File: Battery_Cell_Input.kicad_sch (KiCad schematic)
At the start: 27 parts, among them J1101 Battery_1, J1102 Conn_01x02, Q1101 NMOS, Q1102 NMOS, U1101 BQ76920PW

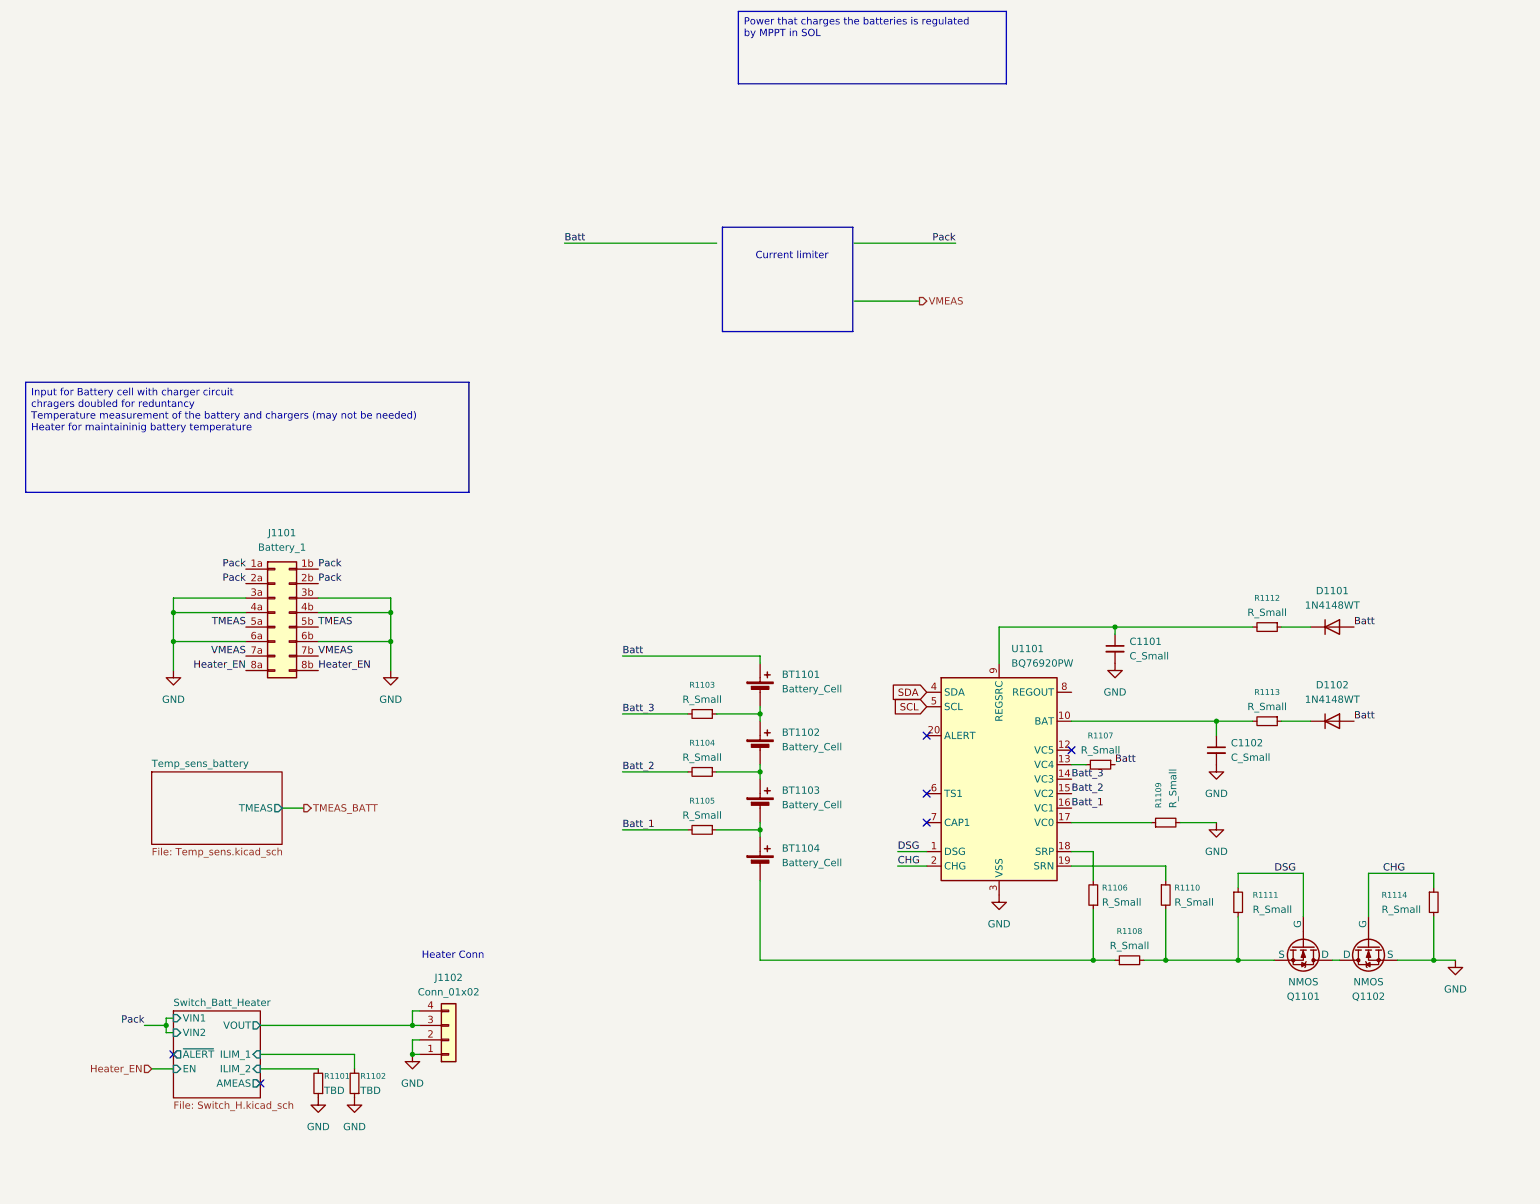
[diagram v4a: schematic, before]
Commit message: updated battery pack module; updated solar inputs module
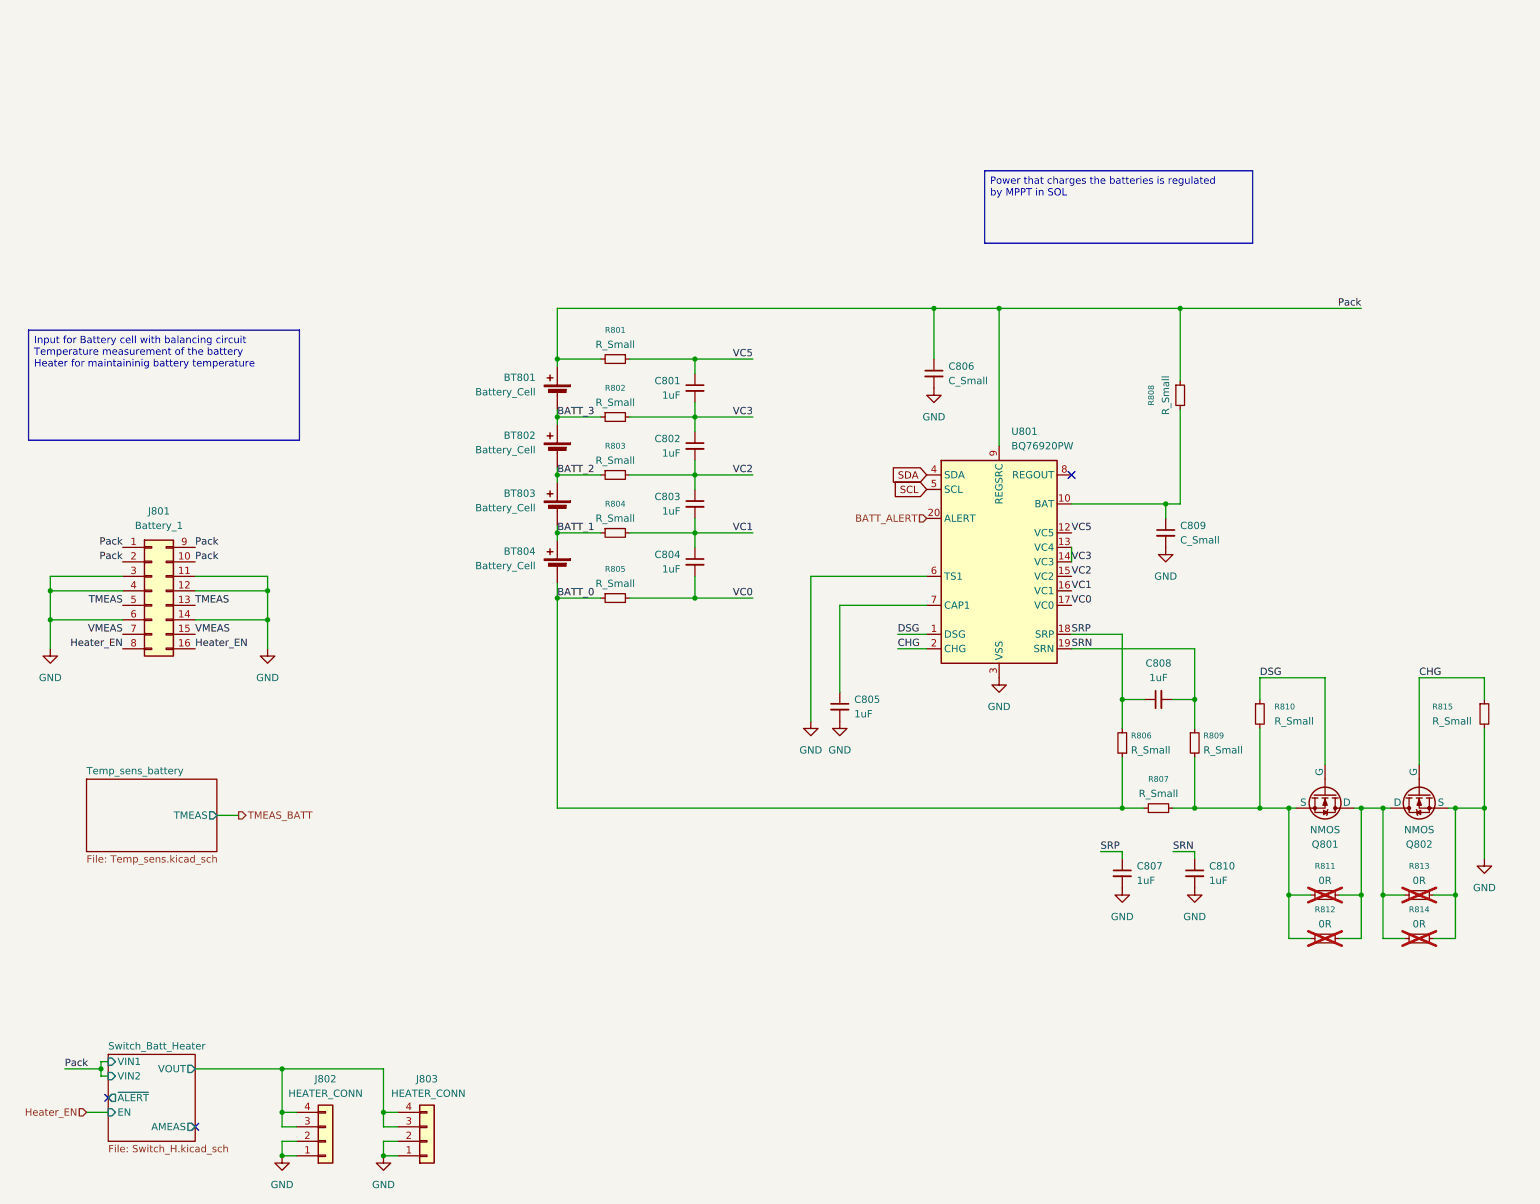
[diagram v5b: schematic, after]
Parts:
- removed D1101, D1102: 1N4148WT, Diode_SMD:D_SOD-523, symbol Diode:1N4148WT
- removed R1101, R1102: TBD, Resistor_SMD:R_0603_1608Metric_Pad0.98x0.95mm_HandSolder, symbol Device:R_Small
- removed R1109, R1112: R_Small, Resistor_SMD:R_0603_1608Metric_Pad0.98x0.95mm_HandSolder, symbol Device:R_Small
- added C801, C802, C803, C804, C805, C807, C808, C810: 1uF, Capacitor_SMD:C_0603_1608Metric_Pad1.08x0.95mm_HandSolder, symbol Device:C_Small
- added J803: HEATER_CONN, symbol Connector_Generic:Conn_01x04
- added R805: R_Small, Resistor_SMD:R_0603_1608Metric_Pad0.98x0.95mm_HandSolder, symbol Device:R_Small
- added R811, R812, R813, R814: 0R, Resistor_SMD:R_0603_1608Metric_Pad0.98x0.95mm_HandSolder, symbol Device:R_Small
- BT801: renamed from BT1101; footprint (none) -> Outlines:BHC186501P-li-ion
- BT802: renamed from BT1102; footprint (none) -> Outlines:BHC186501P-li-ion
- BT803: renamed from BT1103; footprint (none) -> Outlines:BHC186501P-li-ion
- BT804: renamed from BT1104; footprint (none) -> Outlines:BHC186501P-li-ion
- J801: renamed from J1101; symbol Connector_Generic:Conn_02x08_Row_Letter_Last -> Connector_Generic:Conn_02x08_Top_Bottom
- J802: renamed from J1102; value Conn_01x02 -> HEATER_CONN
- Q801: renamed from Q1101; footprint Package_TO_SOT_SMD:SOT-23-6 -> Outlines:NVTFS5116PLTWG
- Q802: renamed from Q1102; footprint Package_TO_SOT_SMD:SOT-23-6 -> Outlines:NVTFS5116PLTWG
- renumbered C1101 to C806, C1102 to C809, R1107 to R801, R1103 to R802, R1104 to R803, R1105 to R804, R1106 to R806, R1108 to R807, R1113 to R808, R1110 to R809, R1111 to R810, R1114 to R815, U1101 to U801
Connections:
- net Batt_3 is gone; now on net VC3: R802.2, U801.14 (VC3)
- net GND: now also J801.11 (Pin_11), J801.12 (Pin_12), J801.14 (Pin_14), J801.3 (Pin_3), J801.4 (Pin_4), J801.6 (Pin_6), U801.6 (TS1), C805.2, C807.2, C810.2, J803.1 (Pin_1), J803.2 (Pin_2), R813.2, R814.2; no longer J801.3a (Pin_3a), J801.3b (Pin_3b), J801.4a (Pin_4a), J801.4b (Pin_4b), J801.6a (Pin_6a), J801.6b (Pin_6b)
- net Heater_EN: now also J801.16 (Pin_16), J801.8 (Pin_8); no longer J801.8a (Pin_8a), J801.8b (Pin_8b)
- net Pack: now also BT801.1 (+), C806.1, J801.1 (Pin_1), J801.10 (Pin_10), J801.2 (Pin_2), J801.9 (Pin_9), R801.2, R808.1, U801.9 (REGSRC); no longer J801.1a (Pin_1a), J801.1b (Pin_1b), J801.2a (Pin_2a), J801.2b (Pin_2b)
- net Switch_Batt_Heater/VOUT: now also J803.3 (Pin_3), J803.4 (Pin_4)
- net TMEAS: now also J801.13 (Pin_13), J801.5 (Pin_5); no longer J801.5a (Pin_5a), J801.5b (Pin_5b)
- net VMEAS: now also J801.15 (Pin_15), J801.7 (Pin_7); no longer J801.7a (Pin_7a), J801.7b (Pin_7b)
- net at Q801.3 (S), R807.2, R809.2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: now also R811.1, R812.1
- net SRN: now reaches R809.1, U801.19 (SRN)
- net SRN: now also C808.2, C810.1
- net BATT_1: now reaches BT803.2 (-), BT804.1 (+), R804.1
- net at Q801.1 (D), Q802.1 (D): now also R811.2, R812.2, R813.1, R814.1
- net BATT_2: now reaches BT802.2 (-), BT803.1 (+), R803.1
- net BATT_0: now reaches BT804.2 (-), R806.1, R807.1
- net BATT_0: now also R805.1
- net BATT_3: now reaches BT801.2 (-), BT802.1 (+), R802.1
- net VC5: now reaches U801.12 (VC5)
- net VC5: now also R801.1, C801.1
- net VC3: now reaches U801.13 (VC4)
- net VC3: now also C801.2, C802.1; no longer R801.2
- net VC0: now reaches U801.17 (VC0)
- net VC0: now also C804.2, R805.2
- net SRP: now reaches R806.2, U801.18 (SRP)
- net SRP: now also C807.1, C808.1
- net BATT_ALERT: now reaches U801.20 (ALERT)
- net at U801.7 (CAP1): now also C805.1
- removed net Batt: BT801.1 (+), R801.1
- net Batt_1 renamed VC1
- net VC1: now also C803.2, C804.1
- net Batt_2 renamed VC2
- net VC2: now also C802.2, C803.1
- no-connect marks 6 -> 3
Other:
- sheet Switch_Batt_Heater ports: added none; removed ILIM_1, ILIM_2
- note removed: "Current limiter"
- note removed: "Heater Conn"
- moved on the sheet: BT801, BT802, BT803, BT804, C806, C809, J801, J802, Q801, Q802, R801, R802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

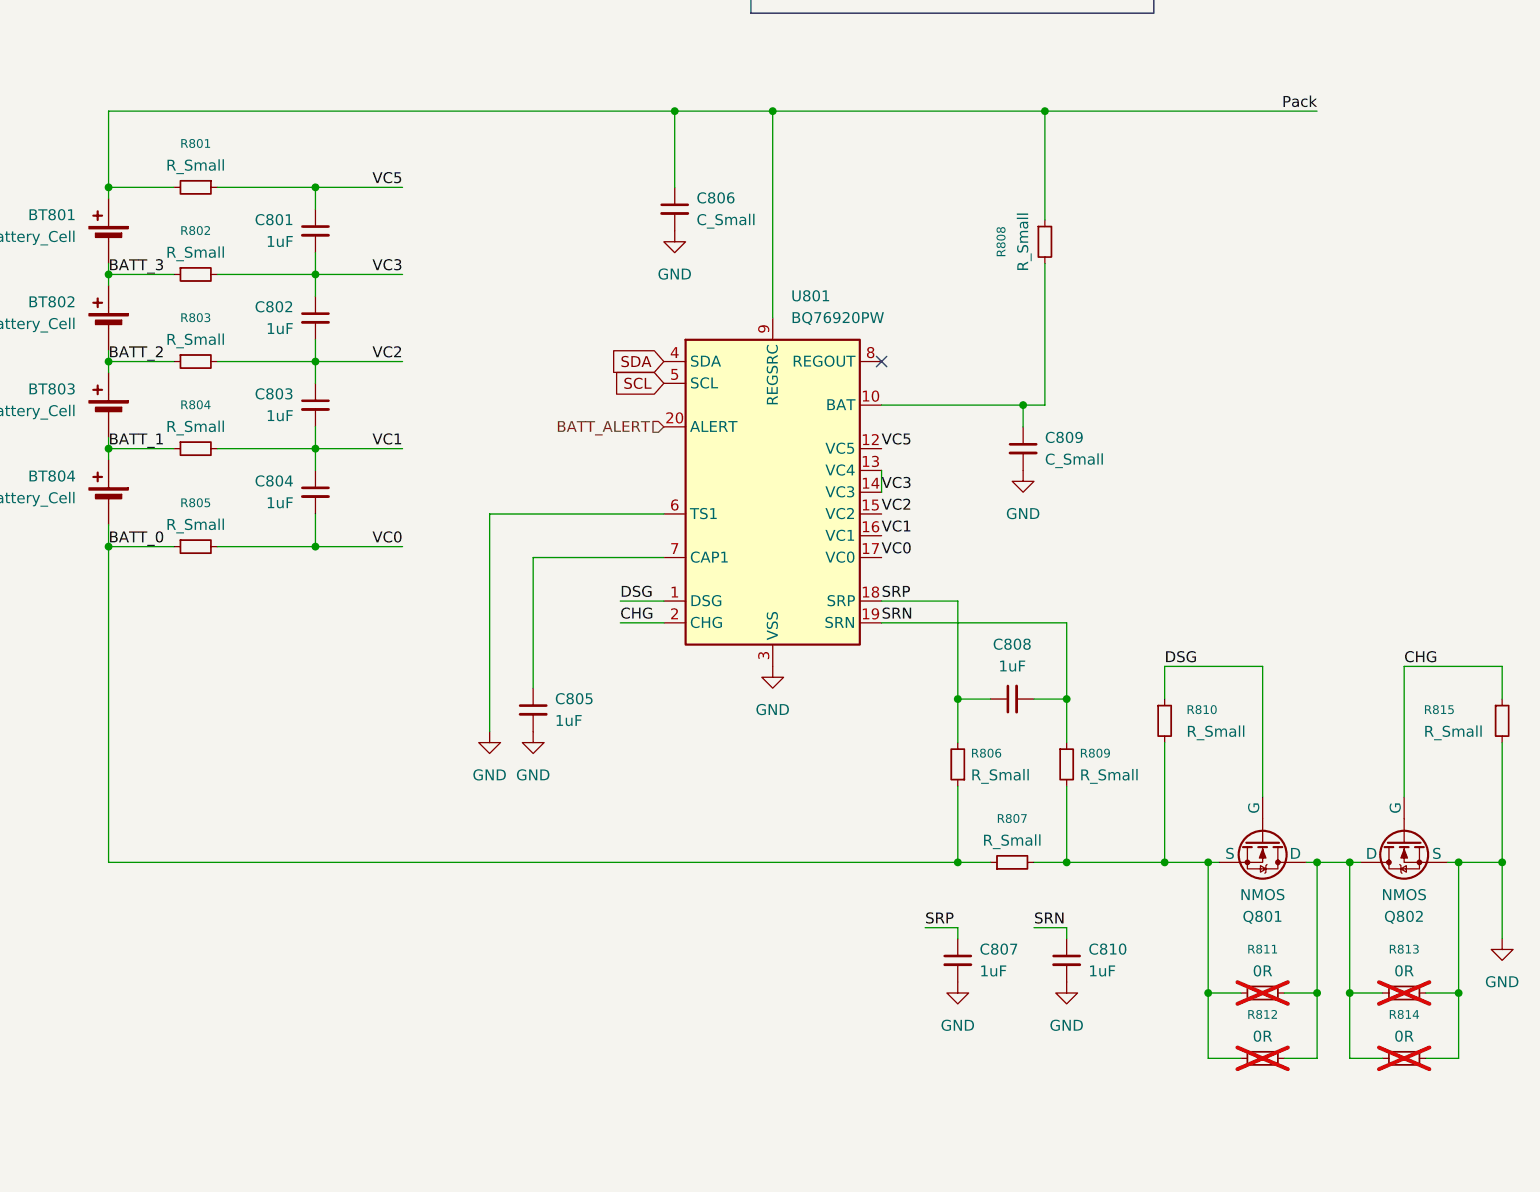
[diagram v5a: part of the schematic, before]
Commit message: added values to most parts
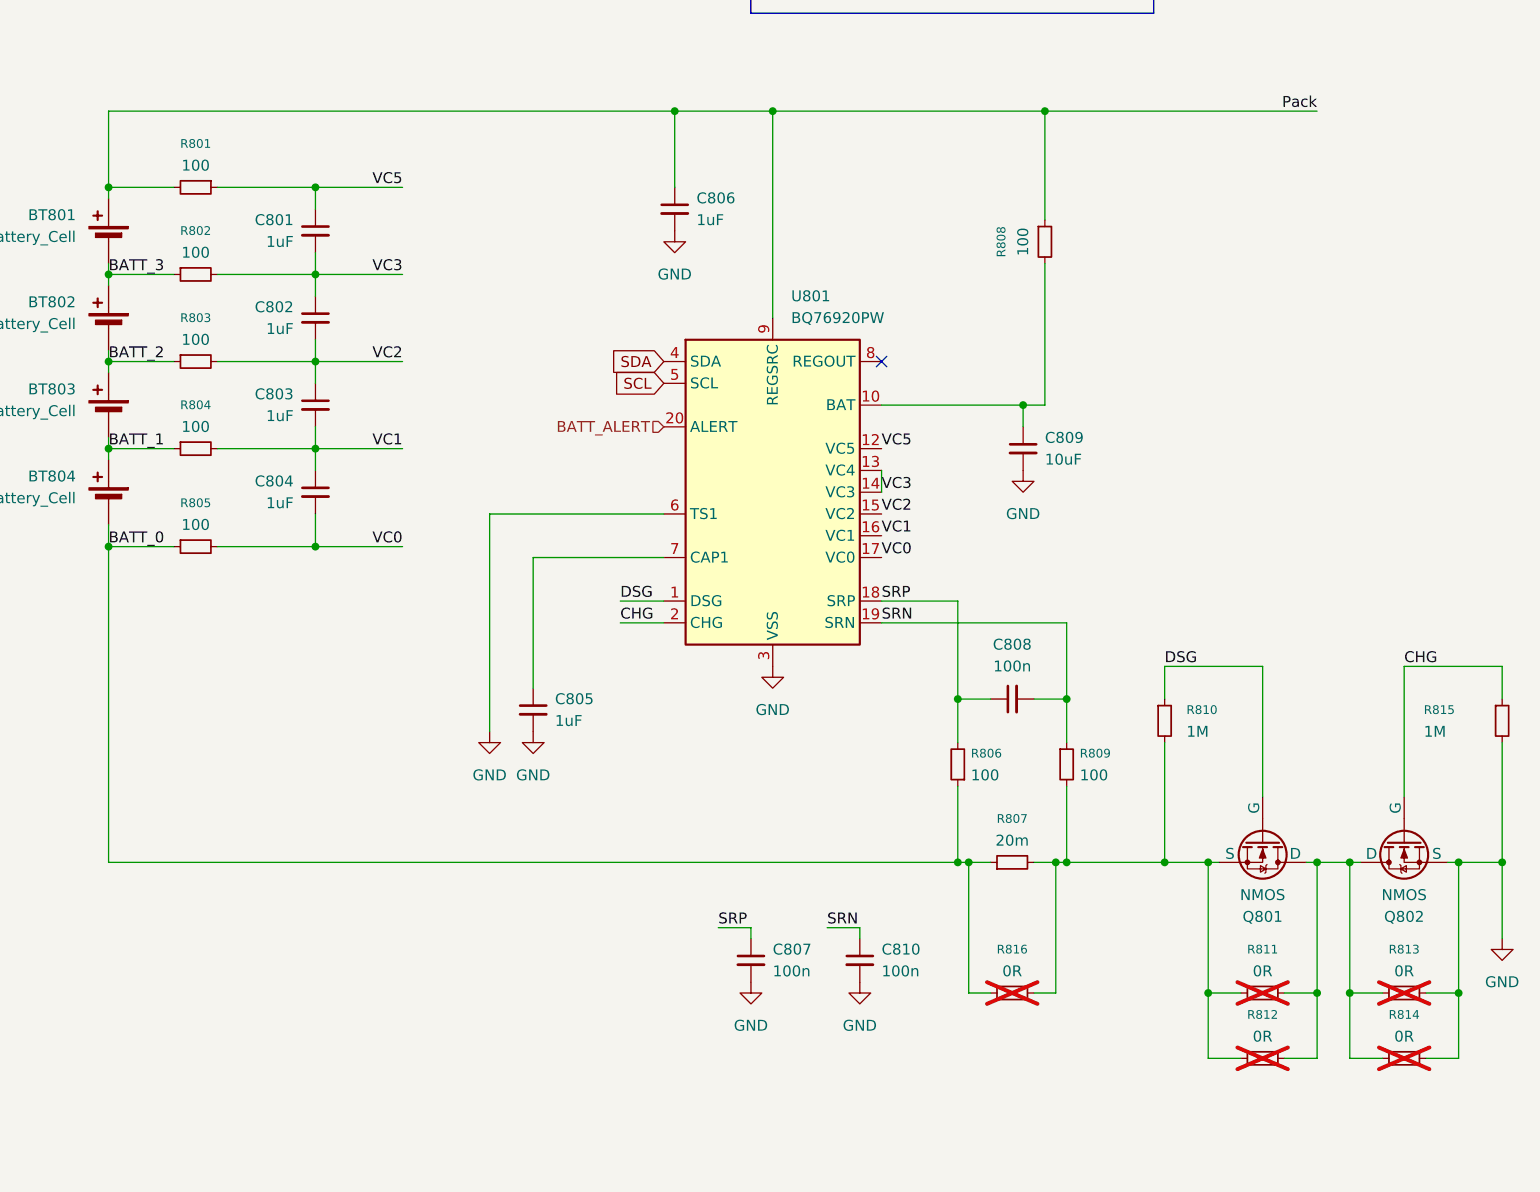
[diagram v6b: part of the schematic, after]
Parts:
- added R816: 0R, Resistor_SMD:R_0603_1608Metric_Pad0.98x0.95mm_HandSolder, symbol Device:R_Small
- C806: value C_Small -> 1uF
- C807, C808, C810: value 1uF -> 100n
- C809: value C_Small -> 10uF
- J802, J803: footprint (none) -> Connector_Molex:Molex_CLIK-Mate_505405-0470_1x04-1MP_P1.50mm_Vertical
- R801, R802, R803, R804, R805, R806, R808, R809: value R_Small -> 100
- R807: value R_Small -> 20m
- R810, R815: value R_Small -> 1M
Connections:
- net BATT_0: now also R816.1
- net at Q801.3 (S), R807.2, R809.2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: now also R816.2
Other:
- moved on the sheet: C807, C810

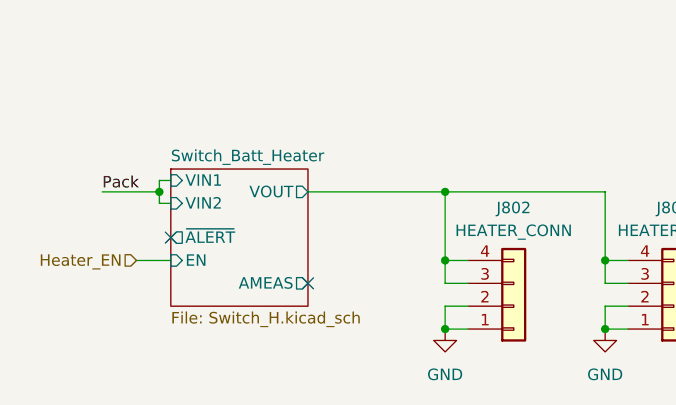
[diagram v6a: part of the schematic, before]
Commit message: deleted unused sheets, added standalone current measure sheet
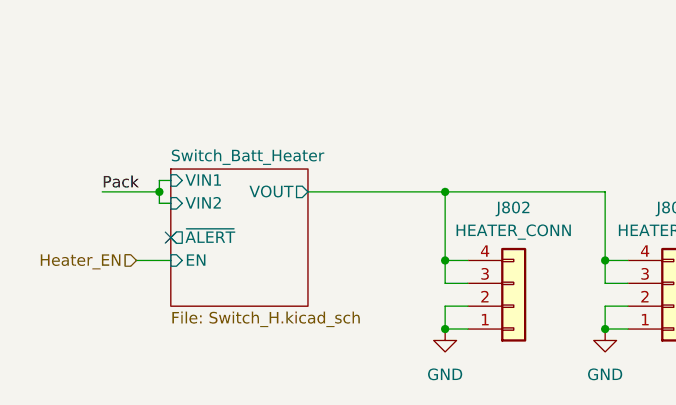
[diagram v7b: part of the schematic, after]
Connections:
- no-connect marks 3 -> 2
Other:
- sheet Switch_Batt_Heater ports: added none; removed AMEAS
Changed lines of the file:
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@@
 	)
 	(no_connect
-		(at 46.99 181.61)
-	)
-	(no_connect
 		(at 200.66 67.31)
 	)
@@
 			)
 		)
-		(pin "AMEAS" output
-			(at 46.99 181.61 0)
-			(effects
-				(font
-					(size 1.27 1.27)
-				)
-				(justify right)
-			)
-		)
